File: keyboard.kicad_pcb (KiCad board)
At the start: 2 copper layers, 75.4 x 113.7 mm, 112 parts, among them IC1 ATMEGA32U4, J1 MINI, P1 MISO, P2 Vcc, P200 GND, P201 GND, P202 GND, P203 GND, P204 GND, P205 GND, P3 SCK, P300 DRL, P301 DRL, P302 DRL, P303 DRL, P304 DRL, P305 DRL, P306 DRL, P307 DRL, P309 DRL, P310 DRL, P311 DRL, P312 DRL, P313 DRL, P314 DRL, P315 DRL, P316 DRL, P317 DRL, P318 DRL, P319 DRL, P4 MOSI, P5 RES, P6 GND, X1 ASX3F

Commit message: v0.8
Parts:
- removed H0, H1: hole, PKRH
- removed P300, P301, P302, P303, P304, P305, P306, P307, P309, P310, P311, P312, P313, P314, P315, P316, P317, P318, P319: DRL, Pad_Drl
- added LOGO1: Geekhack, LOGO, F.Cu at (83.3, 121.4)
- added M1: HOLE, Pad_Drl, F.Cu at (137.7, 159.4)
- added M10: HOLE, Pad_Drl, F.Cu at (98.4, 159.4)
- added M11: HOLE, Pad_Drl, F.Cu at (88.2, 159.4)
- added M12: HOLE, Pad_Drl, F.Cu at (84.4, 159.4)
- added M13: HOLE, Pad_Drl, F.Cu at (80.6, 159.4)
- added M14: HOLE, Pad_Drl, F.Cu at (76.8, 159.4)
- added M15: HOLE, Pad_Drl, F.Cu at (73.0, 159.4)
- added M16: HOLE, Pad_Drl, F.Cu at (65.3, 159.4)
- added M17: HOLE, Pad_Drl, F.Cu at (62.3, 159.4)
- added M2: HOLE, Pad_Drl, F.Cu at (133.9, 159.4)
- added M3: HOLE, Pad_Drl, F.Cu at (125.0, 159.4)
- added M4: HOLE, Pad_Drl, F.Cu at (121.2, 159.4)
- added M5: HOLE, Pad_Drl, F.Cu at (117.4, 159.4)
- added M6: HOLE, Pad_Drl, F.Cu at (113.6, 159.4)
- added M7: HOLE, Pad_Drl, F.Cu at (109.8, 159.4)
- added M8: HOLE, Pad_Drl, F.Cu at (106.0, 159.4)
- added M9: HOLE, Pad_Drl, F.Cu at (102.2, 159.4)
- added P10: ROW4, Pad_50mil, B.Cu at (63.6, 89.1)
- added P11: ROW5, Pad_50mil, B.Cu at (63.6, 90.3)
- added P12: ROW6, Pad_50mil, B.Cu at (63.6, 91.6)
- added P13: COL1, Pad_50mil, B.Cu at (63.6, 94.1)
- added P14: COL2, Pad_50mil, B.Cu at (63.6, 95.4)
- added P15: COL3, Pad_50mil, B.Cu at (63.6, 96.7)
- added P16: COL4, Pad_50mil, B.Cu at (63.6, 97.9)
- added P17: FNLED, Pad_50mil, B.Cu at (63.6, 100.5)
- added P18: Vcc, Pad_50mil, B.Cu at (63.6, 101.8)
- added P19: GND, Pad_50mil, B.Cu at (63.6, 103.0)
- added P7: ROW1, Pad_50mil, B.Cu at (63.6, 85.2)
- added P8: ROW2, Pad_50mil, B.Cu at (63.6, 86.5)
- added P9: ROW3, Pad_50mil, B.Cu at (63.6, 87.8)
- H2: footprint PKRHSL -> Mechanical_Slot
- J1: footprint 67503 -> USB_MINI-B_MOLEX_67503-1020
- P200, P201, P202, P203, P204, P205: footprint Pad-Gnd -> Pad_Gnd
- RF1, RF2, RF3: moved to F.Cu
- moved D21 13.7 mm to (74.0, 176.7)
- moved S0 1.91 mm to (100.0, 71.9), turned to 90 degrees
- moved D22 1.27 mm to (97.5, 176.7)
- moved D5 0.93 mm to (74.6, 156.4), turned to 180 degrees
- moved P200 0.64 mm to (63.2, 157.6)
- moved D6 0.38 mm to (95.6, 80.2)
- moved D20 0.13 mm to (134.9, 155.7)
- moved P202 0.13 mm to (136.8, 157.8)
- turned S21 to 180 degrees
- turned S5 to 180 degrees
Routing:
- net /Matrix/col2: track 275.9 -> 160.1 mm, vias 3 -> 5
- net GND: track 534.5 -> 426.0 mm, vias 28 -> 1
- net VCC: track 314.6 -> 224.0 mm, vias 6 -> 3
- net /Matrix/col4: track 159.2 -> 223.8 mm, vias 4 -> 1
- net /Matrix/row5: track 133.3 -> 185.0 mm, vias 0 -> 2
- net N-0000037: track 94.2 -> 46.4 mm, vias 6 -> 4
- net /Matrix/row6: track 135.3 -> 181.9 mm, vias 1 -> 2
- net /Matrix/row4: track 109.4 -> 155.9 mm, vias 1 -> 2
- net N-0000019: track 55.4 -> 13.7 mm
- net /Matrix/row1: track 107.3 -> 146.9 mm
- net N-0000018: track 86.2 -> 51.9 mm, vias 5 -> 4
- net /GPIO0: track 63.6 -> 44.3 mm
- net /Matrix/numlock: track 56.6 -> 75.3 mm
- net /Matrix/col1: track 172.0 -> 153.7 mm, vias 3 -> 5
- net /Matrix/row3: track 112.2 -> 129.9 mm
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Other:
- board text added: "Programmable Keypad"
- board text added: "Rev 0.8"

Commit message: v0.9
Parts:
- added H1: HOLE, Mechanical_Slotted_Hole, F.Cu at (81.0, 83.3)
- added H3: HOLE, Mechanical_Slotted_Hole, F.Cu at (81.0, 140.5)
- added H4: HOLE, Mechanical_Slotted_Hole, F.Cu at (119.1, 140.5)
- added H5: HOLE, Mechanical_Slotted_Hole, F.Cu at (100.0, 166.1)
- H2: footprint Mechanical_Slot -> Mechanical_Slotted_Hole
- RF1, RF2, RF3: moved to B.Cu
- moved H2 67.0 mm to (119.1, 83.3)
- moved RF3 12.5 mm to (120.1, 72.5), turned to 270 degrees
- moved RF2 7.63 mm to (107.0, 82.3), turned to 0 degrees
- moved R1 3.69 mm to (80.7, 77.1), turned to 180 degrees
- moved R2 3.45 mm to (84.5, 77.5)
- moved D21 2.32 mm to (74.4, 174.4), turned to 180 degrees
- moved C8 2.16 mm to (79.8, 74.2)
- moved D22 2.16 mm to (97.5, 174.5)
- moved D5 1.05 mm to (74.4, 155.4), turned to 0 degrees
- moved D16 0.80 mm to (133.4, 79.4)
- moved D1 0.80 mm to (76.3, 79.4)
- moved D11 0.80 mm to (114.4, 79.4)
- moved D6 0.80 mm to (95.3, 79.4)
- moved R4 0.25 mm to (68.9, 82.5), turned to 180 degrees
- moved RF1 0.25 mm to (95.6, 82.5)
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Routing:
- net GND: track 426.0 -> 497.6 mm, vias 1 -> 5
- net VCC: track 224.0 -> 290.8 mm
- net /Matrix/row1: track 146.9 -> 113.6 mm, vias 1 -> 0
- net /GPIO2: track 52.3 -> 84.3 mm
- net N-0000054: track 13.3 -> 34.7 mm
- net N-0000020: track 51.9 -> 32.4 mm, vias 4 -> 2
- net /Matrix/col2: track 160.1 -> 144.5 mm, vias 5 -> 3
- net /~RES~: track 67.1 -> 82.7 mm, vias 2 -> 1
- net /Matrix/row3: track 129.9 -> 114.5 mm
- net /MISO: track 33.3 -> 23.2 mm, vias 0 -> 1
- net N-0000051: track 14.7 -> 24.8 mm
- net N-0000037: track 46.4 -> 37.8 mm, vias 4 -> 2
- net /Matrix/row2: track 115.6 -> 107.0 mm
- net /Matrix/col3: track 176.8 -> 183.7 mm, vias 3 -> 1
- net N-0000019: track 56.0 -> 62.7 mm, vias 2 -> 0
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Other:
- board text added: "Expansion Pinout on Reverse"
- board text added: "FOR S1 LED"
- board text added: "FOR S11 LED"
- board text added: "FOR S16 LED"
- board text added: "FOR S6 LED"
- board text added: "Rev 0.9"
- board text added: "S1"
- board text added: "S11"
- board text added: "S16"
- board text added: "S1LED"
- board text added: "S6"
- board text added: "Score both sides deeply then cut (or break carefully)"
- board text added: "Special thanks to komar007, bpiphany and Regack"
- board text added: "or D171"
- board text added: "or D181"
- board text added: "or D191"
- board text added: "or D201"
- board text added: "orD211"
- board text added: "orD51"
- board text removed: "CAPS"
- board text removed: "ESC"
- board text removed: "Rev 0.8"

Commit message: v0.12
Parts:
- added P20: SCLM, Pad_50mil, B.Cu at (63.6, 104.3)
- added P21: SDAM, Pad_50mil, B.Cu at (63.6, 105.6)
- added R6: 2.2kΩ, SM0805, B.Cu at (81.0, 132.9)
- added R7: 2.2kΩ, SM0805, B.Cu at (81.0, 130.3)
- added U1: MCP23018, adafruit-SSOP24, B.Cu at (68.3, 123.4)
- C1, C2: value 22p -> 22pF
- C3, C8: value 1u -> 1uF
- C4, C5, C6, C7: value 100n -> 0.1uF
- D1, D10, D11, D12, D13, D14, D15, D16, D17, D18, D19, D2, D20, D21, D22, D23, D24, D3, D4, D5, D6, D7, D8, D9: footprint SM0805D -> SOD-123
- H1, H2, H3, H4, H5: footprint Mechanical_Slotted_Hole -> Mechanical_Hole
- J1: value MINI -> MINI-B
- R1, R2: value 22 -> 22Ω
- R3, R5: value 10k -> 10kΩ
- R4: value 300 -> kΩ
- RF1, RF2, RF3: value R -> kΩ
- S0: value DTSM-6 -> ADTSMW69NVTR
- X1: value ASX3F -> 7M-16.000MAAJ-T
- moved D24 10.8 mm to (131.5, 164.9), turned to 270 degrees
- moved D23 10.7 mm to (112.6, 164.9), turned to 270 degrees
- moved D21 9.85 mm to (76.9, 164.9), turned to 270 degrees
- moved D22 9.77 mm to (95.9, 164.9), turned to 270 degrees
- moved D20 9.44 mm to (131.8, 146.8), turned to 270 degrees
- moved D17 9.44 mm to (131.8, 89.7), turned to 270 degrees
- moved D18 9.44 mm to (131.8, 108.7), turned to 270 degrees
- moved D19 9.44 mm to (131.8, 127.8), turned to 270 degrees
- moved D10 1.42 mm to (98.1, 155.7)
- moved D4 1.42 mm to (75.2, 136.7)
- moved D9 1.42 mm to (94.3, 136.7)
- moved D12 1.42 mm to (113.3, 98.6)
- moved D13 1.42 mm to (113.3, 106.2)
- moved D2 1.42 mm to (75.2, 98.6)
- moved D7 1.42 mm to (94.3, 98.6)
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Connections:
- D17 pad 1: N-0000055 (its old number) -> /Matrix/col4
- D17 pad 2: /Matrix/col4 -> N-0000065
- D18 pad 1: N-0000050 -> /Matrix/col4
- D18 pad 2: /Matrix/col4 -> N-0000061
- D19 pad 1: N-0000053 -> /Matrix/col4
- D19 pad 2: /Matrix/col4 -> N-0000063
- D20 pad 1: N-0000052 -> /Matrix/col4
- D20 pad 2: /Matrix/col4 -> N-0000060
- S17 pad 2: N-0000055 (its old number) -> N-0000065
- S171 pad 2: N-0000055 (its old number) -> N-0000065
- S18 pad 2: N-0000050 -> N-0000061
- S181 pad 2: N-0000050 -> N-0000061
- S19 pad 2: N-0000053 -> N-0000063
- S191 pad 2: N-0000053 -> N-0000063
- S20 pad 2: N-0000052 -> N-0000060
- S201 pad 2: N-0000052 -> N-0000060
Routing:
- net GND: track 497.6 -> 605.9 mm, vias 5 -> 13
- net /Matrix/row5: track 182.8 -> 258.7 mm
- net N-0000047: track 62.7 -> 131.0 mm, vias 0 -> 2
- net /Matrix/row2: track 107.0 -> 164.3 mm, vias 0 -> 3
- net VCC: track 290.8 -> 341.9 mm, vias 3 -> 9
- net N-0000048: track 58.7 -> 106.6 mm, vias 0 -> 2
- net /Matrix/col3: track 183.7 -> 224.3 mm, vias 1 -> 3
- net /SCLM: track 0.00 -> 40.1 mm, vias 0 -> 2
- net /Matrix/row3: track 114.5 -> 153.4 mm, vias 1 -> 3
- net /Matrix/row1: track 113.6 -> 151.3 mm, vias 0 -> 3
- net /SDAM: track 0.00 -> 35.9 mm, vias 0 -> 3
- net /Matrix/col2: track 144.5 -> 164.6 mm, vias 3 -> 1
- net /GPIO1: track 45.9 -> 64.3 mm, vias 2 -> 0
- net N-000005: track 15.5 -> 32.4 mm
- net /GPIO2: track 84.3 -> 67.9 mm
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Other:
- outline, holes or cut-outs redrawn
- net class Default: clearance 0.2 -> 0.18; trace_width 0.2 -> 0.18
- net class POWER: trace_width 0.508 -> 0.5
- rule trace_clearance: 0.2 -> 0.18
- rule trace_min: 0.2 -> 0.18
- rule via_min_size: 1 -> 0.8
- board text added: "MCP23018"
- board text added: "Never install the serial expander and ATMEGA at the same time... but you knew that already."
- board text added: "Programmable, Expandable, Alterable & Enviable Keypad"
- board text added: "Rev 0.12"
- board text added: "Special thanks to komar007, Dox, bpiphany and Regack"
- board text removed: "Programmable Keypad"
- board text removed: "Rev 0.9"
- board text removed: "Special thanks to komar007, bpiphany and Regack"

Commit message: v0.12.1
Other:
- board text added: "R6 & R7 only used by MCP23018"
- board text added: "Rev 0.12.1"
- board text removed: "Rev 0.12"

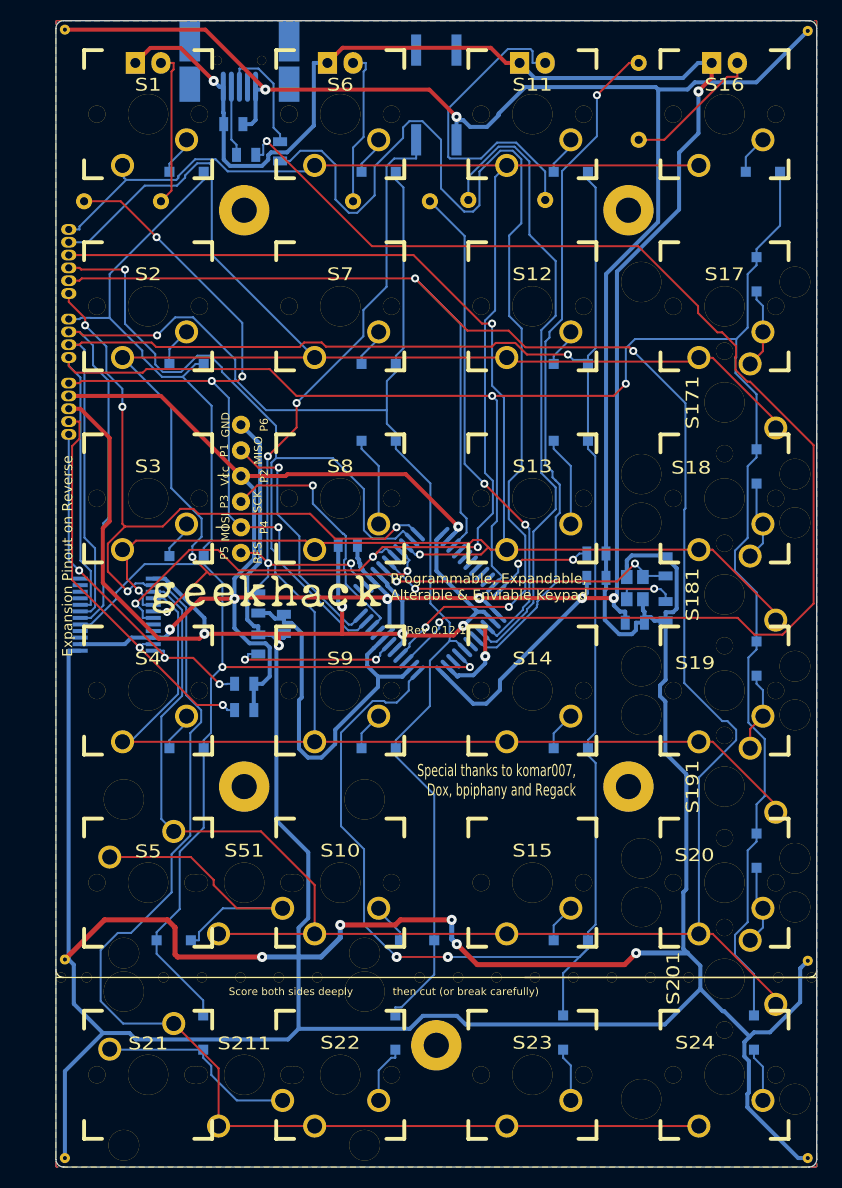
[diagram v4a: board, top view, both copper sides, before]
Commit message: 4x5 variant
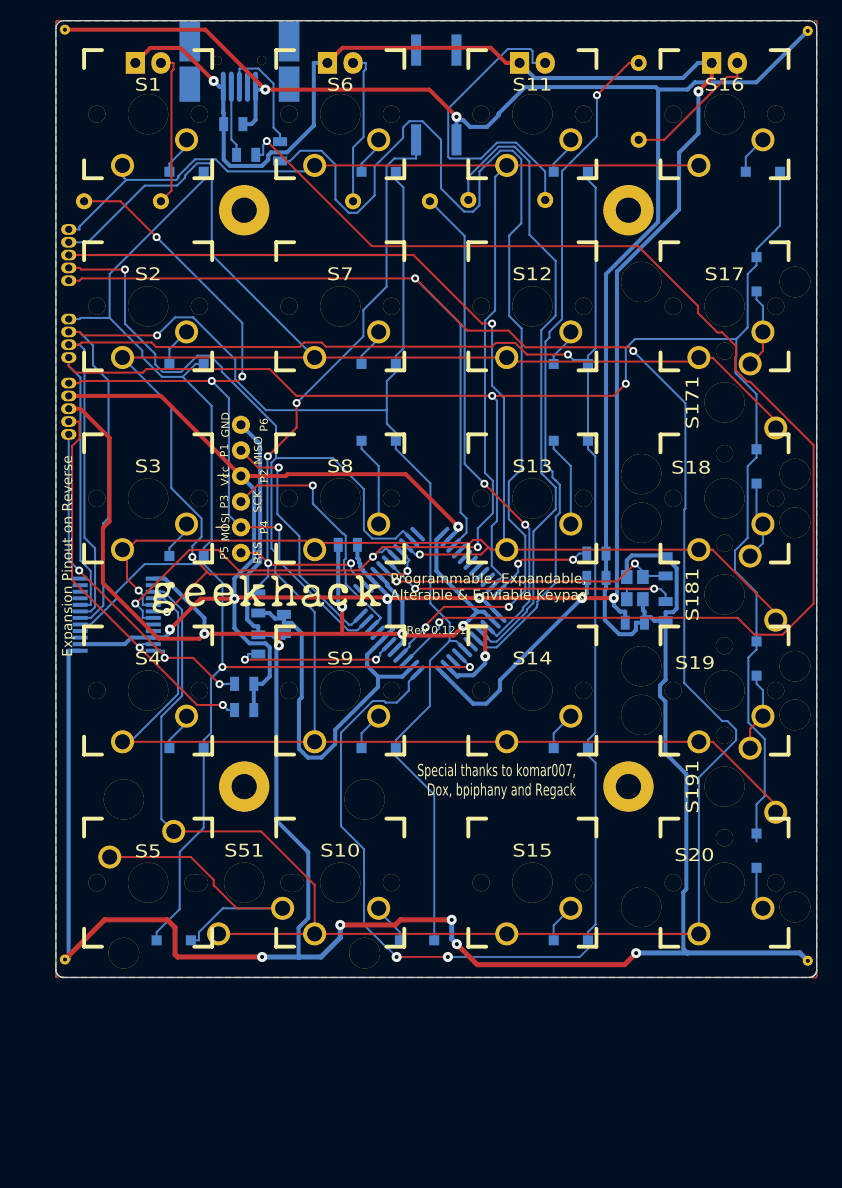
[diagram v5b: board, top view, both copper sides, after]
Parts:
- removed D21, D22, D23, D24: 1N4148, SOD-123
- removed H5: HOLE, Mechanical_Hole
- removed M1, M10, M11, M12, M13, M14, M15, M16, M17, M2, M3, M4, M5, M6, M7, M8, M9: HOLE, Pad_Drl
- removed P12: ROW6, Pad_50mil
- removed P204, P205: GND, Pad_Gnd
- removed S201, S211: MX1A, CHERRY_PCB_200H_Visible
- removed S21, S22, S23, S24: MX1A, CHERRY_PCB_100H_Plated
- J1: value MINI-B -> USB MINI-B
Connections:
- IC1 pad 22: /Matrix/row6 -> (no net)
- U1 pad 2: /Matrix/row6 -> (no net)
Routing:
- net /Matrix/row6: track 184.7 -> 0.00 mm, vias 4 -> 0
- net GND: track 605.9 -> 488.7 mm
- net N-0000062 (its old number): track 20.2 -> 0.00 mm
- net /Matrix/col4: track 210.5 -> 191.6 mm
- net /Matrix/row5: track 258.7 -> 247.7 mm
- net /Matrix/col2: track 164.6 -> 155.2 mm
- net /Matrix/col1: track 146.6 -> 137.2 mm
- net /Matrix/col3: track 224.3 -> 215.8 mm
- net N-0000056 (its old number): track 5.95 -> 0.00 mm
- net N-0000055 (its old number): track 5.40 -> 0.00 mm
- net N-0000054: track 5.35 -> 0.00 mm
- net N-0000062: track 7.98 -> 4.28 mm
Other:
- board size 75.4 x 113.7 mm -> 75.4 x 94.9 mm
- board text removed: "Score both sides deeply then cut (or break carefully)"
- board text removed: "orD211"

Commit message: v0.12.2
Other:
- board text added: "Rev 0.12.2"
- board text removed: "Rev 0.12.1"

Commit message: fixed silkscreen
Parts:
- turned D5 to 0 degrees
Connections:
- D5 pad 1: N-0000066 (its old number) -> /Matrix/col1
- D5 pad 2: /Matrix/col1 -> N-0000065
- S5 pad 2: N-0000066 (its old number) -> N-0000065
- S51 pad 2: N-0000066 (its old number) -> N-0000065
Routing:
- net N-0000066 (its old number): track 30.4 -> 0.00 mm
- net N-0000065: track 0.00 -> 30.4 mm

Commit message: v0.12.3
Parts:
- D1, D10, D11, D12, D13, D14, D15, D16, D17, D18, D19, D2, D20, D3, D4, D5, D6, D7, D8, D9: footprint SOD-123 -> SOD-123(A-C)
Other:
- board text added: "Rev 0.12.3"
- board text removed: "Rev 0.12.2"
